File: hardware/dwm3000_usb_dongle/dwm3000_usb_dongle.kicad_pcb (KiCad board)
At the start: 2 copper layers, 355 x 140 mm, 20 parts, among them J1 USB_A_Neltron_5075AR-04, J2 BoxHeader_2x05_P1.27mm_CnCTec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, U1 TSSOP-20_4.4x6.5mm_P0.65mm, U2 SOT-23-5

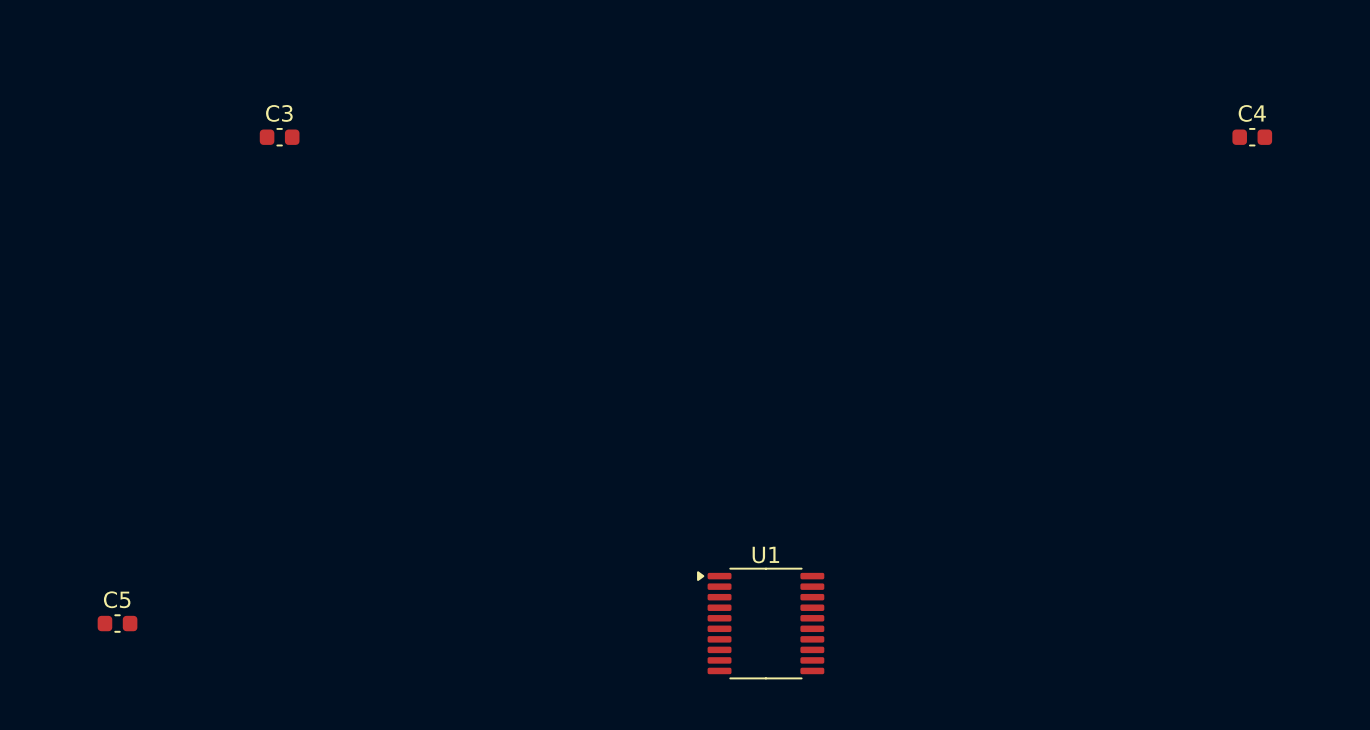
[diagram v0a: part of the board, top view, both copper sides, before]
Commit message: Switch MCU from STM32F042F6P6 to STM32C071F8P6
Same TSSOP20 footprint, but a materially different pinout that required
re-wiring the schematic:

- USB_DM/USB_DP now land on native PA11/PA12 (pins 16/17) -- no
  SYSCFG_CFGR1.PA11_PA12_RMP remap needed like the F042 required.
- This package has no NRST pin at all (traded for one more GPIO), so J2's
  SWD nRESET (pin 10) is now no-connect and the NRST filter cap is removed.
  Debuggers reset via software (AIRCR.SYSRESETREQ) instead.
- No separate VDDA pin either -- single VDD/VSS supply, so one 100nF
  decoupling cap instead of two.
- Re-mapped SPI1/DWM3000 control/LED signals onto the new pin numbers,
  keeping the same net names throughout.

STM32C071 isn't in this KiCad 7.0.11 install's bundled symbol library (it
was added upstream after this KiCad release, in a newer generator format
7.0.11 can't parse), so extra_symbols/STM32C071F8Px.kicad_sym vendors the
real upstream symbol as the source of truth for the pin table, and
gen_sch.py reproduces those pins in the older KiCad-7-compatible syntax.

Regenerated the netlist, schematic PDF, and the placed-footprint PCB;
verified the netlist's 16 signal nets + no-connects match the new pinout.

Co-Authored-By: Claude Sonnet 5 <noreply@anthropic.com>
Claude-Session: https://claude.ai/code/session_0115nx7Q2HiGYnps6zk84N7F
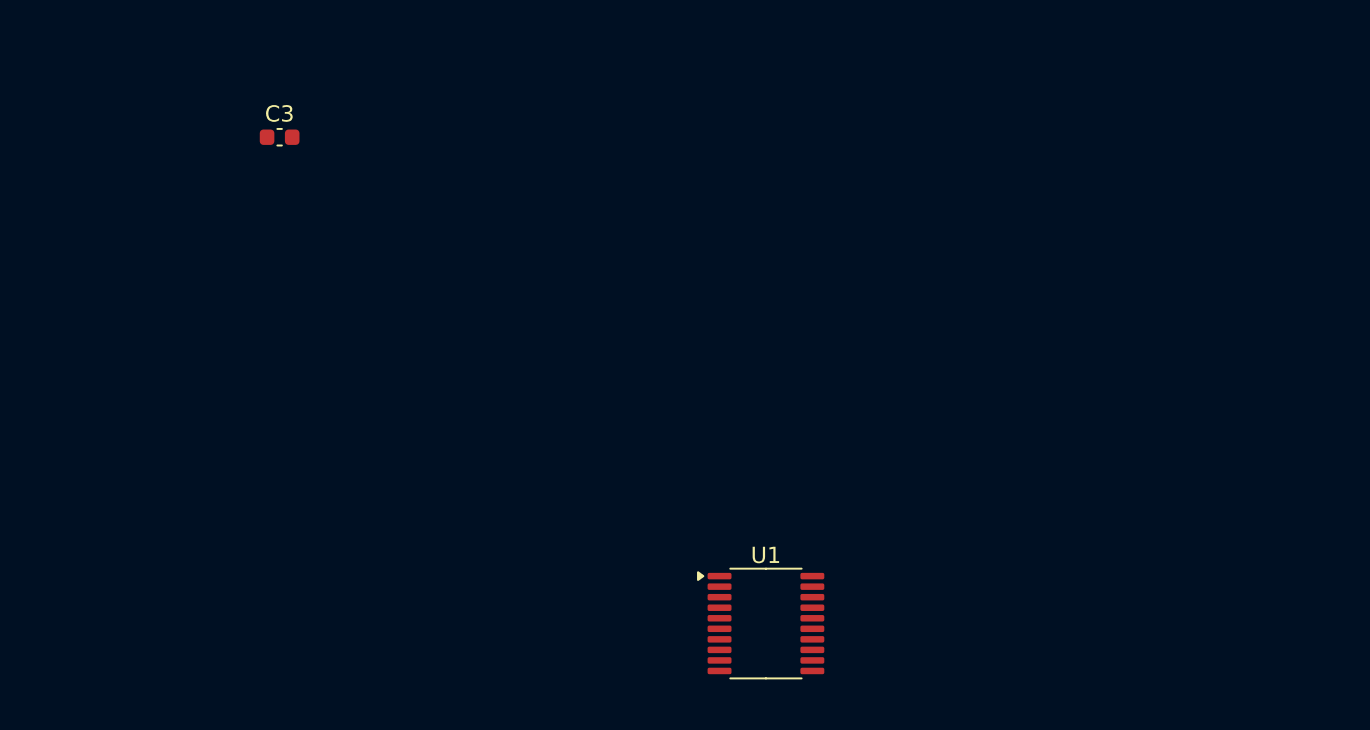
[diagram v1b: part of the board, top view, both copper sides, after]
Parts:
- removed C4, C5: C_0603_1608Metric, C_0603_1608Metric
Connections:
- J2 pad 10: /NRST -> unconnected-(J2-Pin_10-Pad10)
- U1 pad 10: unconnected-(U1-PA4-Pad10) -> /SPI_CS
- U1 pad 11: /SPI_SCK -> unconnected-(U1-PA4-Pad11)
- U1 pad 12: /SPI_MISO -> /SPI_SCK
- U1 pad 13: /SPI_MOSI -> /SPI_MISO
- U1 pad 14: unconnected-(U1-PB1-Pad14) -> /SPI_MOSI
- U1 pad 15: GND -> unconnected-(U1-PA8-Pad15)
- U1 pad 16: +3V3 -> /USB_DM_MCU
- U1 pad 17: /USB_DM_MCU -> /USB_DP_MCU
- U1 pad 18: /USB_DP_MCU -> /SWDIO
- U1 pad 19: /SWDIO -> /SWCLK
- U1 pad 20: /SWCLK -> unconnected-(U1-PB3/PB4/PB5/PB6-Pad20)
- U1 pad 4: /NRST -> +3V3
- U1 pad 5: +3V3 -> GND
- U1 pad 6: /DWM_WAKEUP -> unconnected-(U1-PF2-Pad6)
- U1 pad 7: /DWM_RSTN -> /DWM_WAKEUP
- U1 pad 8: /DWM_IRQ -> /DWM_RSTN
- U1 pad 9: /SPI_CS -> /DWM_IRQ

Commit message: Set real component values on PCB silkscreen (was showing bare footprint names)
While re-checking the project after the MCU swap, noticed build_pcb.py never
copied each component's schematic Value onto its placed footprint, so every
part's silkscreen/Fab value text just showed the generic footprint library
name (e.g. "TSSOP-20_4.4x6.5mm_P0.65mm") instead of the actual part (e.g.
"STM32C071F8P6"). This affected all 18 parts, not just the MCU. Now parses
the netlist's (value ...) field and calls FOOTPRINT.SetValue() per part.

Co-Authored-By: Claude Sonnet 5 <noreply@anthropic.com>
Claude-Session: https://claude.ai/code/session_0115nx7Q2HiGYnps6zk84N7F
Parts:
- C1, C2: value C_0805_2012Metric -> 10uF
- C3, C7: value C_0603_1608Metric -> 100nF
- C6: value C_0603_1608Metric -> 1uF
- D1, D2, D3: value LED_0603_1608Metric -> LED
- DWM1: value DWM1000 -> DWM3000
- J1: value USB_A_Neltron_5075AR-04 -> USB-4AM103AS
- J2: value BoxHeader_2x05_P1.27mm_CnCTech_3221 -> 3221-10-0300-00
- R1, R2: value R_0603_1608Metric -> 22R
- R3: value R_0603_1608Metric -> 1k
- R4, R5: value R_0603_1608Metric -> 330R
- U1: value TSSOP-20_4.4x6.5mm_P0.65mm -> STM32C071F8P6
- U2: value SOT-23-5 -> XC6220B331MR-G

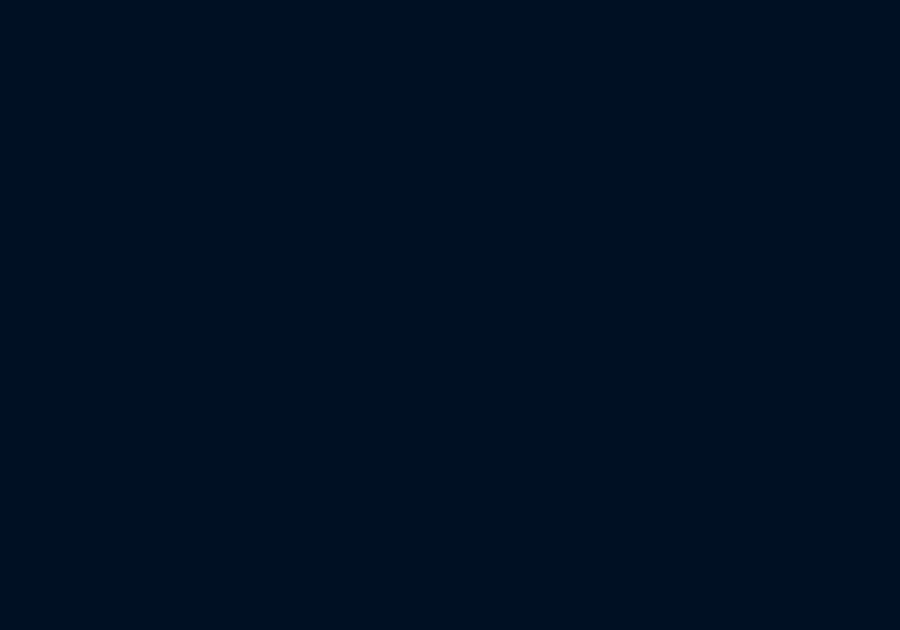
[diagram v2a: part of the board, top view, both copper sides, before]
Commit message: Add DNP-by-default optional USB D+ pull-up (R6)
STM32C071's internal USB D+ pull-up almost certainly makes this
unnecessary -- every ST full-speed USB device peripheral in this IP
family (F0/G0/L0/C0) has had a software-controlled internal pull-up
(USB_BCDR.DPPU) -- but st.com wasn't reachable from here to confirm it
against the STM32C071 reference manual directly, so this adds a
footprint-only safety net instead of leaving it unresolved.

R6 (1.5k, USB_DP_MCU to +3V3, right at the R2/PA12 side) is placed on the
schematic and PCB with dnp=yes: it shows the standard DNP cross in the
schematic and is excluded from BOM/position files on the board, so normal
assembly doesn't populate it. Only stuff it if bring-up shows the device
isn't enumerating as full-speed.

Co-Authored-By: Claude Sonnet 5 <noreply@anthropic.com>
Claude-Session: https://claude.ai/code/session_0115nx7Q2HiGYnps6zk84N7F
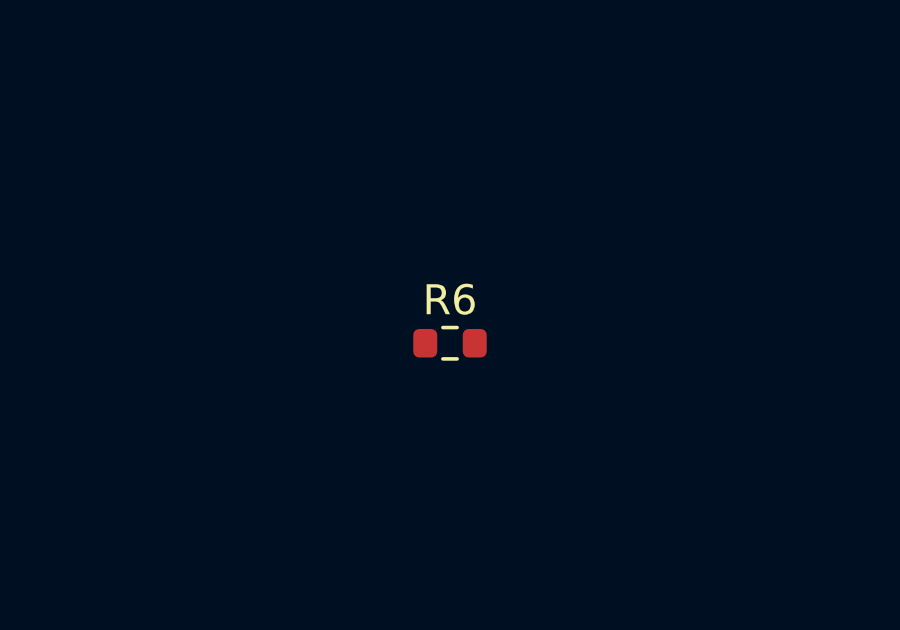
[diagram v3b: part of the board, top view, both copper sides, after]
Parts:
- added R6: DNP 1.5k (see README: only if MCU lacks an internal USB D+ 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, R_0603_1608Metric, F.Cu at (170.0, 90.0)

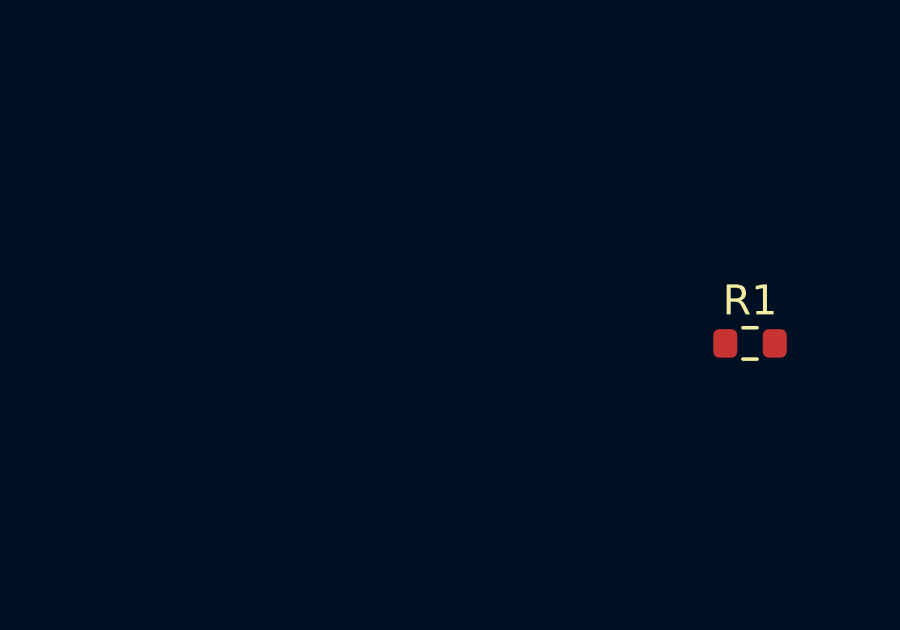
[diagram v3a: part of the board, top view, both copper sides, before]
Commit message: Fix: wire STM32 pin 6 (PF2-NRST) to SWD nRESET -- it is NOT a plain GPIO
A previous revision claimed the STM32C071F8Px TSSOP20 package "has no NRST
pin at all" and left both the MCU pin and J2's nRESET unconnected. That was
wrong. Pin 6 is named PF2-NRST in ST's own pin database (confirmed against
the public STM32_open_pin_data repo): it defaults to acting as a normal
reset input, and is only reassignable to plain PF2 GPIO via the
NRST_MODE[1:0] option byte (which this design does not set).

The KiCad symbol used to build extra_symbols/STM32C071F8Px.kicad_sym only
lists this pin's ordinary alternate functions (PF2/RCC_MCO/TIM1_CH4) since
the reset/GPIO duality is option-byte-controlled, not a normal AF, so it
never showed up in that pin table -- that's what led to the earlier mistake.

Fix: pin 6 is wired to J2 pin 10 (nRESET) like a normal NRST, with a 100nF
filter cap (C5) per ST's usual hardware design guidelines (AN2586). Hardware
connect-under-reset now works normally. README corrected with the real
mechanism and a pointer to ST's community-documented pitfalls of ever
reassigning this pin to GPIO mode.

Co-Authored-By: Claude Sonnet 5 <noreply@anthropic.com>
Claude-Session: https://claude.ai/code/session_0115nx7Q2HiGYnps6zk84N7F
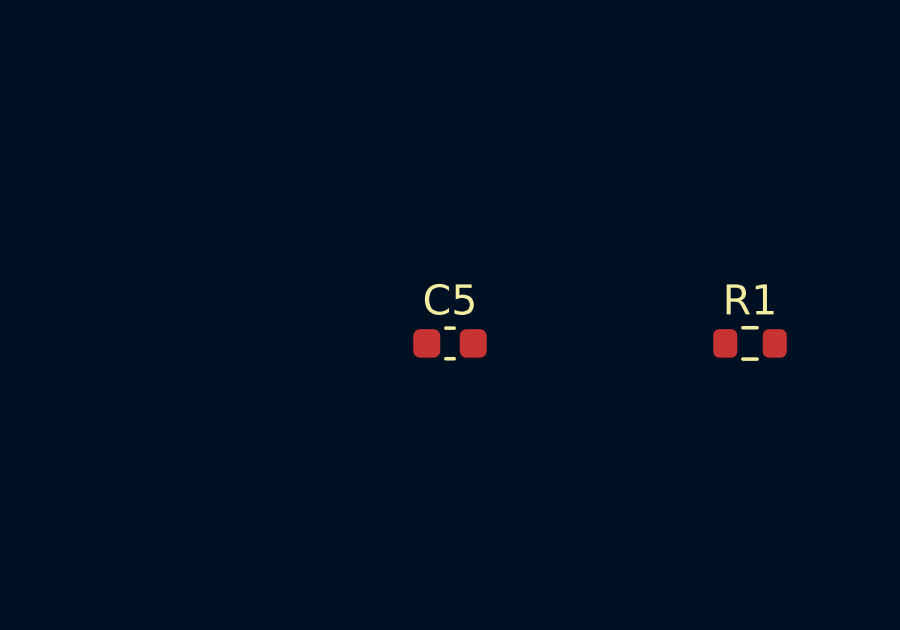
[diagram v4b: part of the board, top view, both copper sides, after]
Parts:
- added C5: 100nF, C_0603_1608Metric, F.Cu at (120.0, 90.0)
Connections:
- J2 pad 10: unconnected-(J2-Pin_10-Pad10) -> /NRST
- U1 pad 6: unconnected-(U1-PF2-Pad6) -> /NRST

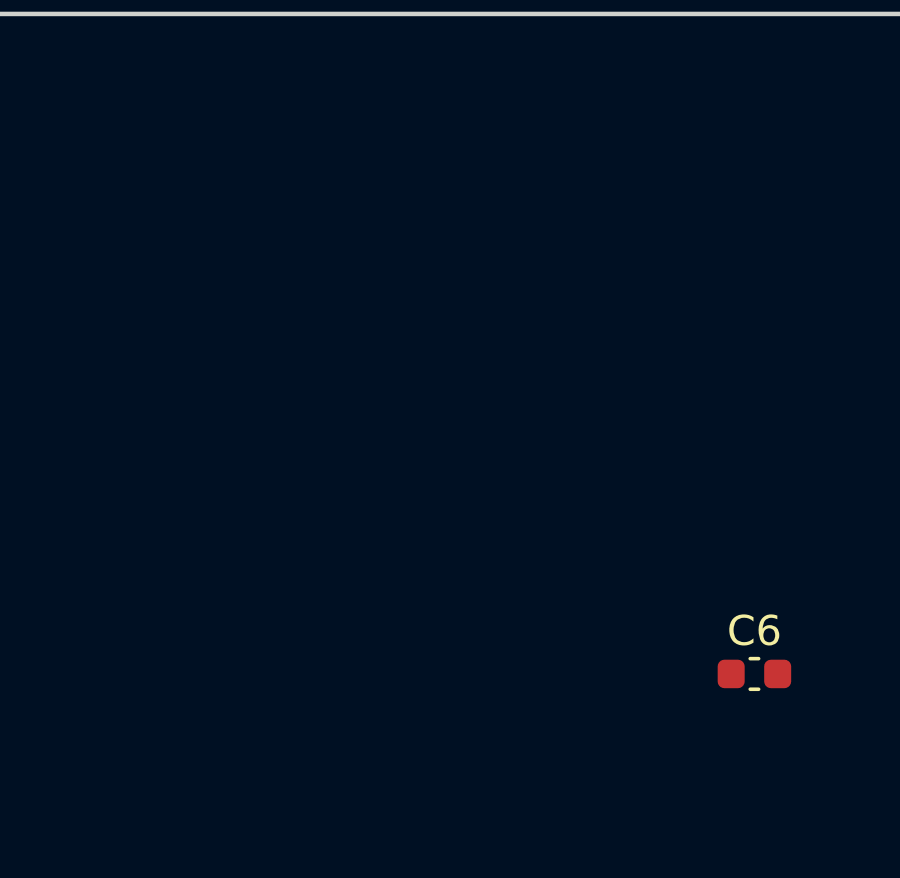
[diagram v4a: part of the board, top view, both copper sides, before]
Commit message: Add second MCU-driven status LED (D4/R7) on STM32 pin 20 (PB3)
Pin 20 is a 4-way multi-bonded pad (PB3/PB4/PB5/PB6 share one physical
pin) selected via the SYSCFG_CFGR3 register -- a normal peripheral
register, not a FLASH option byte like PF2-NRST/PA14-BOOT0, so there's no
unlock sequence or bricking risk: firmware just needs to select PB3 there
before configuring the pin as a GPIO output.

D4 (LED) + R7 (1k series resistor) added following the same +3V3->R->LED
anode->cathode->GPIO(sink) pattern as D1/R3, wired to a new LED2_CTRL net.
README updated (BOM, pin table, and a new explanatory note distinguishing
this ordinary multi-bond selection from the option-byte-special pins
documented earlier).

Co-Authored-By: Claude Sonnet 5 <noreply@anthropic.com>
Claude-Session: https://claude.ai/code/session_0115nx7Q2HiGYnps6zk84N7F
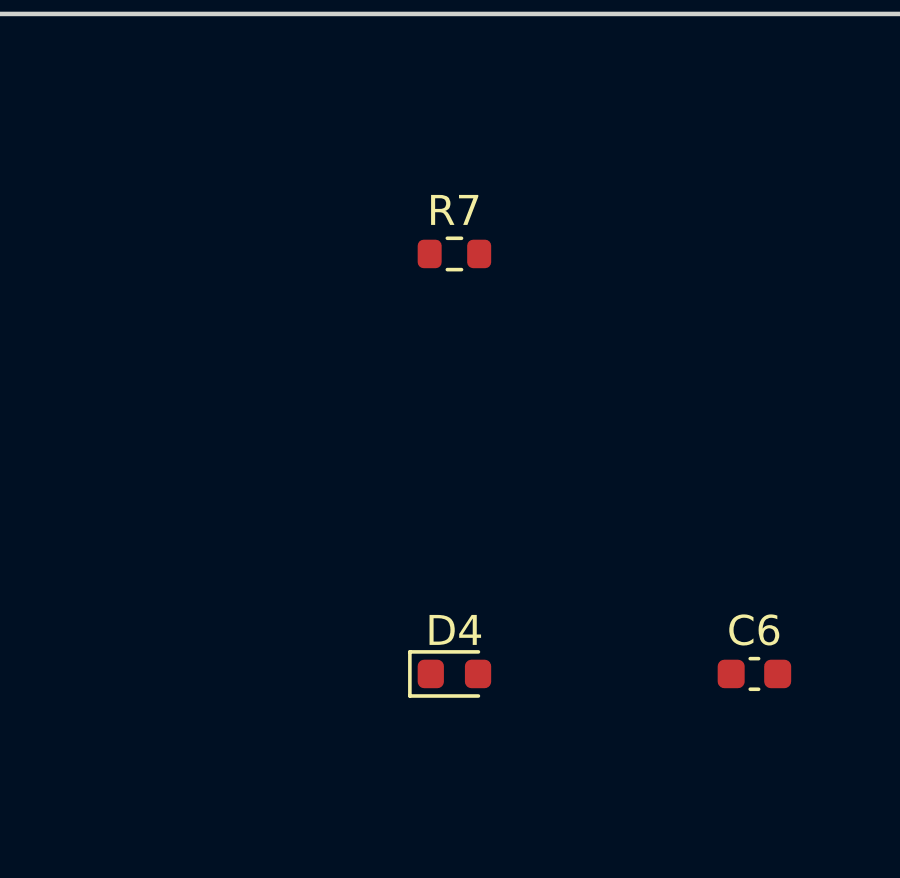
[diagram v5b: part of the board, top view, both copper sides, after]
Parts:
- added D4: LED, LED_0603_1608Metric, F.Cu at (215.0, 32.0)
- added R7: 1k, R_0603_1608Metric, F.Cu at (215.0, 18.0)
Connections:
- U1 pad 20: unconnected-(U1-PB3/PB4/PB5/PB6-Pad20) -> /LED2_CTRL
